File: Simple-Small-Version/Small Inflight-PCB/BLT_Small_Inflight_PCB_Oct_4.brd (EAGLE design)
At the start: 91.2 x 46.5 mm, 7 parts

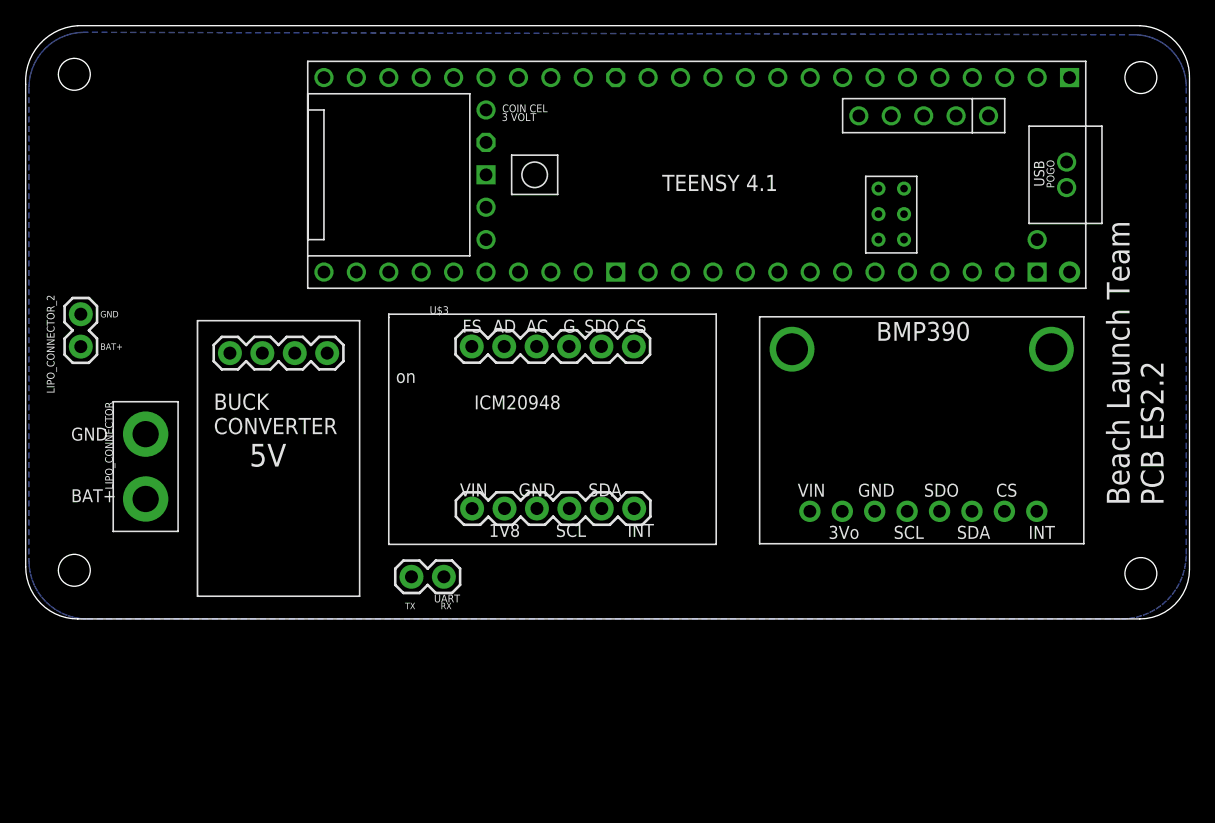
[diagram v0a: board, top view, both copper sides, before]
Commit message: Updated layout
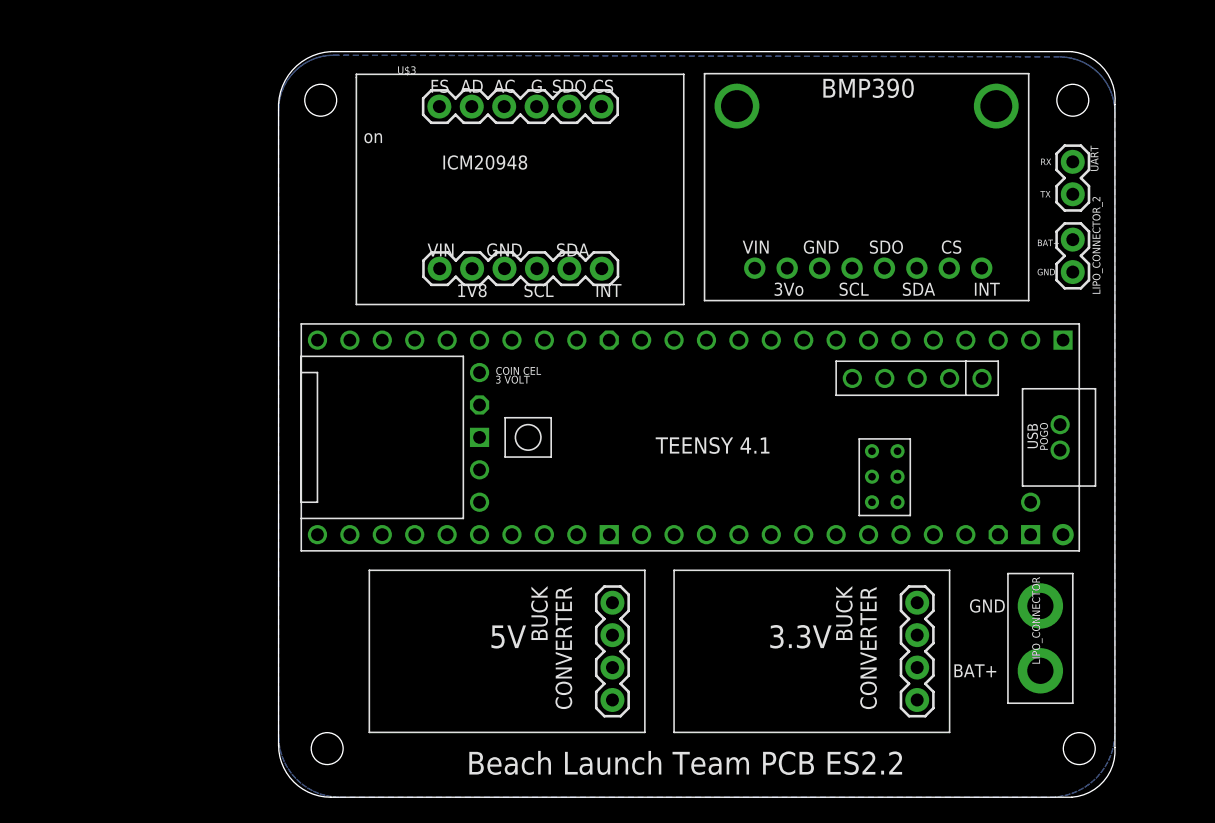
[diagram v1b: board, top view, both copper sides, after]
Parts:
- added U$4: BUCK_CONVERTER3.3V, BLTFootprints:1X04
- moved LIPO_CONNECTOR_2 77.8 mm to (77.2, 77.7), turned to 90 degrees
- moved LIPO_CONNECTOR 71.4 mm to (74.7, 49.0)
- moved UART 59.0 mm to (77.2, 86.4), turned to 270 degrees
- moved U$6 35.8 mm to (41.1, 51.8), turned to 270 degrees
- moved U$1 20.6 mm to (46.0, 64.8)
- moved U$2 19.5 mm to (61.1, 78.0)
- moved U$3 19.0 mm to (18.3, 84.6)
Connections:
- removed net N$3: U$1.3V3-1, U$1.3V3-3
- net 3.3V: now also U$4.VO+; no longer U$1.3V3-2
- net BAT+: now also U$4.IN+
- net GND: now also U$4.GND
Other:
- board size 91.2 x 46.5 mm -> 65.6 x 58.4 mm
- board text added: "3.3V"

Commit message: /
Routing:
- net RX: track 0.00 -> 73.9 mm
- net BAT+: track 0.00 -> 71.6 mm
- net TX: track 0.00 -> 69.0 mm, vias 0 -> 2
- net 3.3V: track 0.00 -> 59.4 mm, vias 0 -> 1
- net SCK: track 0.00 -> 52.6 mm, vias 0 -> 3
- net MISO: track 0.00 -> 44.2 mm, vias 0 -> 1
- net 5V: track 0.00 -> 37.5 mm
- net MOSI: track 0.00 -> 34.6 mm
- net CS2: track 0.00 -> 31.3 mm
- net BMPINT: track 0.00 -> 24.8 mm
- net CS1: track 0.00 -> 21.7 mm, vias 0 -> 1

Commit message: Updated files
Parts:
- removed LIPO_CONNECTOR: (no value), SparkFun-Connectors:1X02_XTRA_BIG
- removed U$4: BUCK_CONVERTER3.3V, BLTFootprints:1X04
- added J1: (no value), SparkFun-Connectors:1X02_XTRA_BIG
- moved U$6 19.1 mm to (60.2, 52.1)
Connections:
- net 3.3V: now also U$1.3V3-1, U$1.3V3-3; no longer U$4.VO+
- net BAT+: now also J1.2; no longer LIPO_CONNECTOR.2, U$4.IN+
- net BMPINT: now also U$1.3-LRCLK2; no longer U$1.20-A6/TX5/LRCLK1
- net CS2: now also U$1.4-BCLK2; no longer U$1.15-A1/RX3/SPDIF_IN
- net GND: now also J1.1; no longer LIPO_CONNECTOR.1, U$4.GND
- net RX: now also U$1.0-RX1/CS1/CRX2; no longer U$1.34-RX8
- net TX: now also U$1.1-TX1/MISO1/CTX2; no longer U$1.35-TX8
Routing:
- net RX: track 73.9 -> 15.3 mm
- net TX: track 69.0 -> 17.3 mm, vias 2 -> 0
- net CS2: track 31.3 -> 7.21 mm
- net BAT+: track 71.6 -> 48.0 mm
- net 5V: track 37.5 -> 18.4 mm
- net BMPINT: track 24.8 -> 7.21 mm
- net 3.3V: track 59.4 -> 62.0 mm, vias 1 -> 2
- net SCK: track 52.6 -> 51.4 mm, vias 3 -> 1
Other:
- board size 65.6 x 58.4 mm -> 65.6 x 54.4 mm
- board text removed: "3.3V"

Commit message: updated files
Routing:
- net 3.3V: track 62.0 -> 60.8 mm
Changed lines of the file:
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@@
 <contactref element="U$1" pad="3V3-1"/>
 <contactref element="U$1" pad="3V3-3"/>
-<wire x1="71.374" y1="57.15" x2="71.374" y2="58.166" width="0.508" layer="1"/>
+<wire x1="71.374" y1="57.15" x2="71.374" y2="57.404" width="0.508" layer="1"/>
 <wire x1="40.894" y1="72.39" x2="38.354" y2="74.93" width="0.508" layer="16"/>
 <wire x1="38.354" y1="74.93" x2="34.544" y2="74.93" width="0.508" layer="16"/>
@@
 <wire x1="27.6098" y1="77.9907" x2="30.6705" y2="74.93" width="0.508" layer="1"/>
 <wire x1="30.6705" y1="74.93" x2="34.544" y2="74.93" width="0.508" layer="1"/>
-<wire x1="44.196" y1="69.088" x2="40.894" y2="72.39" width="0.508" layer="1"/>
-<via x="52.578" y="69.088" extent="1-16" drill="0.35"/>
-<wire x1="52.578" y1="69.088" x2="44.196" y2="69.088" width="0.508" layer="1"/>
-<wire x1="61.3104" y1="68.2296" x2="55.90734375" y2="68.2296" width="0.508" layer="1"/>
-<wire x1="52.578" y1="69.088" x2="55.04894375" y2="69.088" width="0.508" layer="1"/>
-<wire x1="55.90734375" y1="68.2296" x2="55.04894375" y2="69.088" width="0.508" layer="1"/>
-<wire x1="71.374" y1="58.166" x2="61.3104" y2="68.2296" width="0.508" layer="1"/>
+<wire x1="71.374" y1="57.404" x2="60.833" y2="67.945" width="0.508" layer="1"/>
 <wire x1="52.2986" y1="78.0288" x2="52.324" y2="78.0034" width="0.508" layer="16"/>
-<wire x1="52.578" y1="69.088" x2="52.324" y2="69.342" width="0.508" layer="16"/>
-<wire x1="52.324" y1="78.0034" x2="52.324" y2="69.342" width="0.508" layer="16"/>
+<wire x1="52.2986" y1="70.5866" x2="51.816" y2="70.104" width="0.508" layer="16"/>
+<wire x1="52.2986" y1="78.0288" x2="52.2986" y2="70.5866" width="0.508" layer="16"/>
+<via x="51.816" y="70.104" extent="1-16" drill="0.35"/>
+<wire x1="40.894" y1="72.39" x2="43.18" y2="70.104" width="0.508" layer="1"/>
+<wire x1="51.816" y1="70.104" x2="51.816" y2="69.977" width="0.508" layer="1"/>
+<wire x1="53.848" y1="67.945" x2="51.816" y2="69.977" width="0.508" layer="1"/>
+<wire x1="53.848" y1="67.945" x2="60.833" y2="67.945" width="0.508" layer="1"/>
+<wire x1="43.18" y1="70.104" x2="51.816" y2="70.104" width="0.508" layer="1"/>
 </signal>
 <signal name="GND">
